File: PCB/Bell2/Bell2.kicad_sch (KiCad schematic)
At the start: 37 parts, among them J1 USB-C, J2 POWER, J3 Conn_01x10, J4 Shelly, U1 ESP32-PICO-MINI-02, U2 FT231XQ, U3 ISL89410, U4 ISL89410, U5 L96-M33, U6 LMR16006+FB, U7 AA, U8 QR

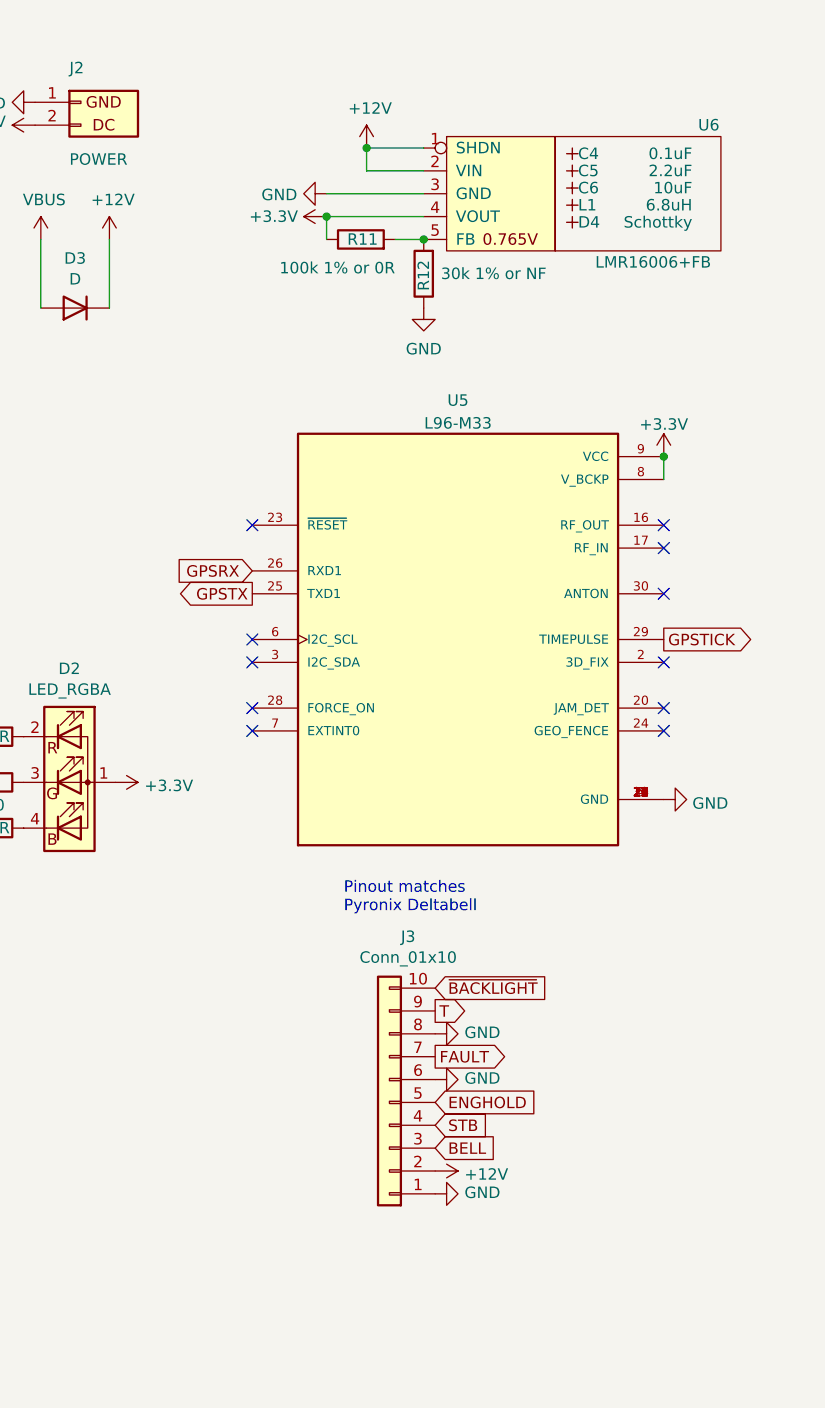
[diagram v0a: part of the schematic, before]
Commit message: New connectors, and separate GPS
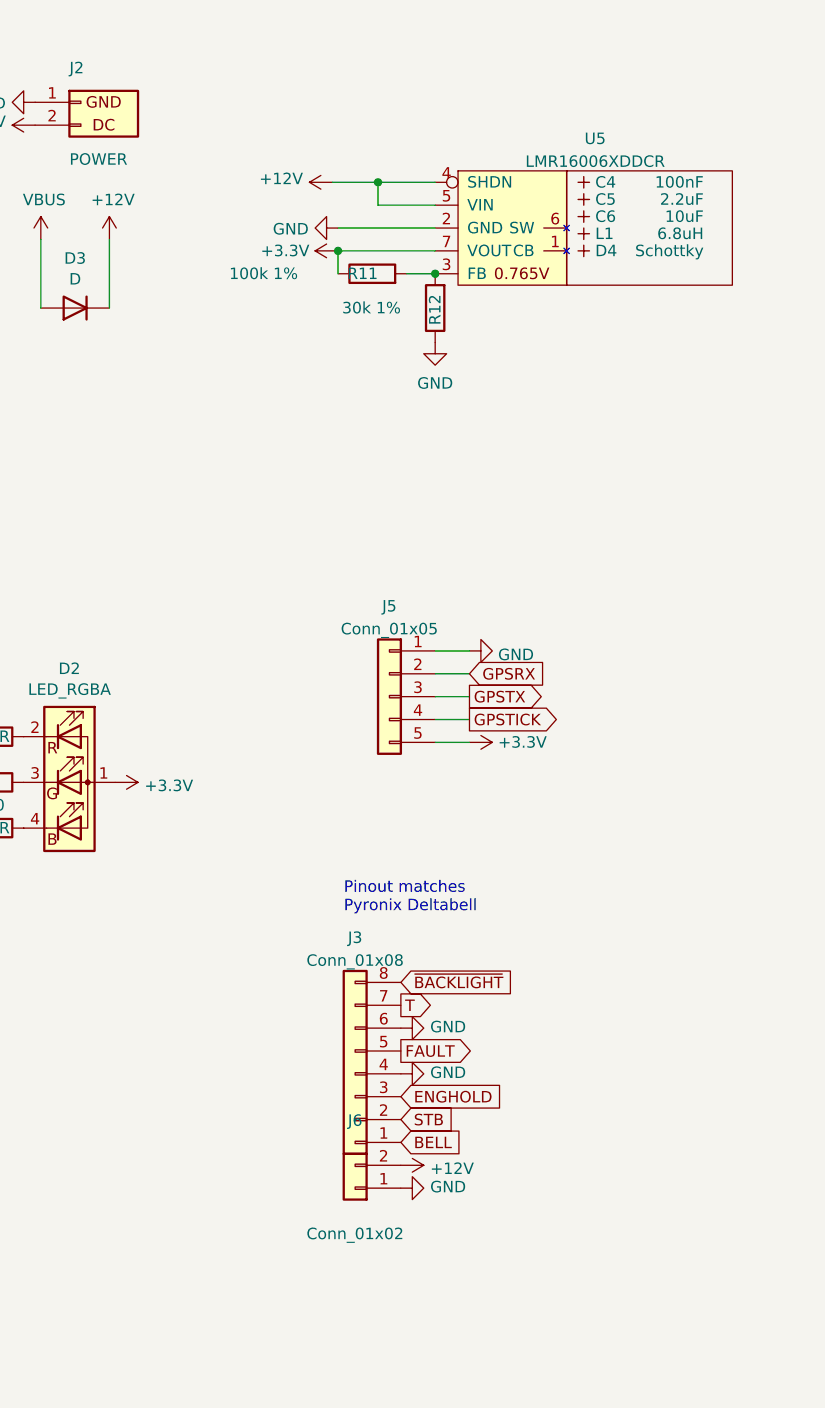
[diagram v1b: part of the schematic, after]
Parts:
- removed J3: Conn_01x10, RevK:Molex_MiniSPOX_H10RA, symbol Connector_Generic:Conn_01x10
- removed U5: L96-M33, RevK:L96-M33, symbol RevK:L96-M33
- removed U6: LMR16006+FB, RevK:SOT-23-Thin-6-Reg, symbol RevK:LMR16006+FB
- added J3: Conn_01x08, RevK:PTSM-HH-8-RA, symbol Connector_Generic:Conn_01x08
- added J5: Conn_01x05, RevK:PTSM-HH-5-RA, symbol Connector_Generic:Conn_01x05
- added J6: Conn_01x02, RevK:PTSM-HH-2-RA, symbol Connector_Generic:Conn_01x02
- added U5: LMR16006XDDCR, RevK:SOT-23-Thin-6-Reg, symbol RevK:LMR16006XDDCR
- C4: value 0.1uF -> 100nF; LCSC Part # (none) -> C30926
- C5: LCSC Part # (none) -> C19110; Note 0603 or 0805 -> (none)
- C6: LCSC Part # (none) -> C17024; Note 0603 or 0805 -> (none)
- D4: JLCPCB Rotation Offset (none) -> 0; LCSC Part # (none) -> C143805; Part No CD1206-B2100 -> (none)
- J2: footprint RevK:Molex_MiniSPOX_H2RA -> RevK:PTSM-HH-2-RA
- L1: LCSC Part # (none) -> C354575; Manufacturer Laird -> (none); Part No TYA4020 -> (none)
- R11: value 100k 1% or 0R -> 100k 1%; LCSC Part # (none) -> C14675
- R12: value 30k 1% or NF -> 30k 1%; LCSC Part # (none) -> C100001
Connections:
- net +12V: now also J6.2 (Pin_2), U5.4 (SHDN), U5.5 (VIN)
- net +3V3: now also J5.5 (Pin_5), U5.7 (VOUT)
- net BELL: now also J3.1 (Pin_1)
- net ENGHOLD: now also J3.3 (Pin_3)
- net FAULT: now also J3.5 (Pin_5)
- net GND: now also J3.4 (Pin_4), J3.6 (Pin_6), J5.1 (Pin_1), J6.1 (Pin_1), U5.2 (GND)
- net GPSRX: now also J5.2 (Pin_2)
- net GPSTICK: now also J5.4 (Pin_4)
- net GPSTX: now also J5.3 (Pin_3)
- net STB: now also J3.2 (Pin_2)
- net T: now also J3.7 (Pin_7)
- net ~{BACKLIGHT}: now also J3.8 (Pin_8)
- net at R11.2, R12.2: now also U5.3 (FB)
- no-connect marks 26 -> 15

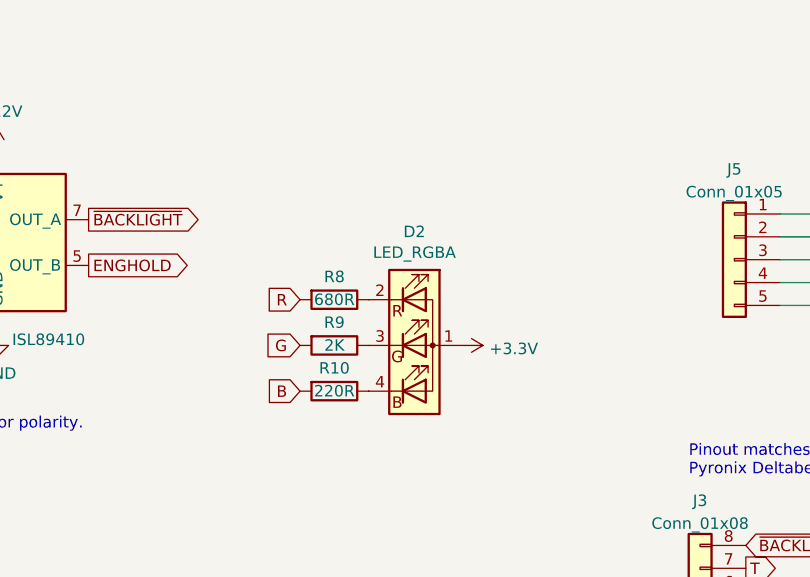
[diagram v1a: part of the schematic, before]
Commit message: New LED
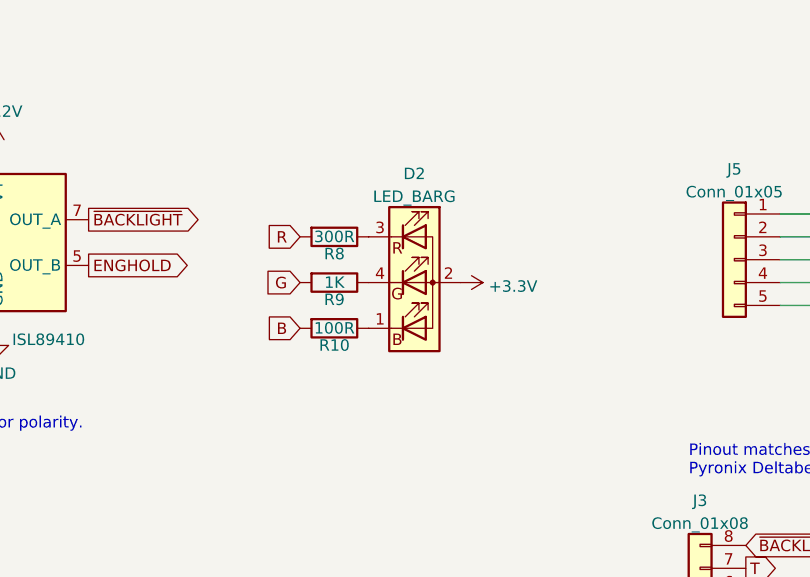
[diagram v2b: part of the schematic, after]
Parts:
- removed D2: LED_RGBA, RevK:LED-RGB-1.6x1.6, symbol Device:LED_ARGB
- added D2: LED_BARG, RevK:MHS190RGBCT, symbol Device:LED_BARG
- R10: value 220R -> 100R; Part No (none) -> 0603-220R
- R8: value 680R -> 300R; Part No (none) -> 0603-680R
- R9: value 2K -> 1K; Part No (none) -> 0603-2K
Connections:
- net +3V3: now also D2.2 (A)
- net at R10.1: now also D2.1 (BK)
- net at R8.1: now also D2.3 (RK)
- net at R9.1: now also D2.4 (GK)
